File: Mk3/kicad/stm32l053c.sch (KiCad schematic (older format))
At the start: 44 parts, among them J1 GND, J10 3V3, J2 GND, J3 TX, J4 GND, J5 TEST_1P, J6 TEST_1P, J7 TEST_1P, J8 RX, J9 3V3, P1 SWD, U1 AP2112, U2 STM32L053C8_LQFP48, U3 ADS1015, U4 UFL_SMA, U5 RFM92/95

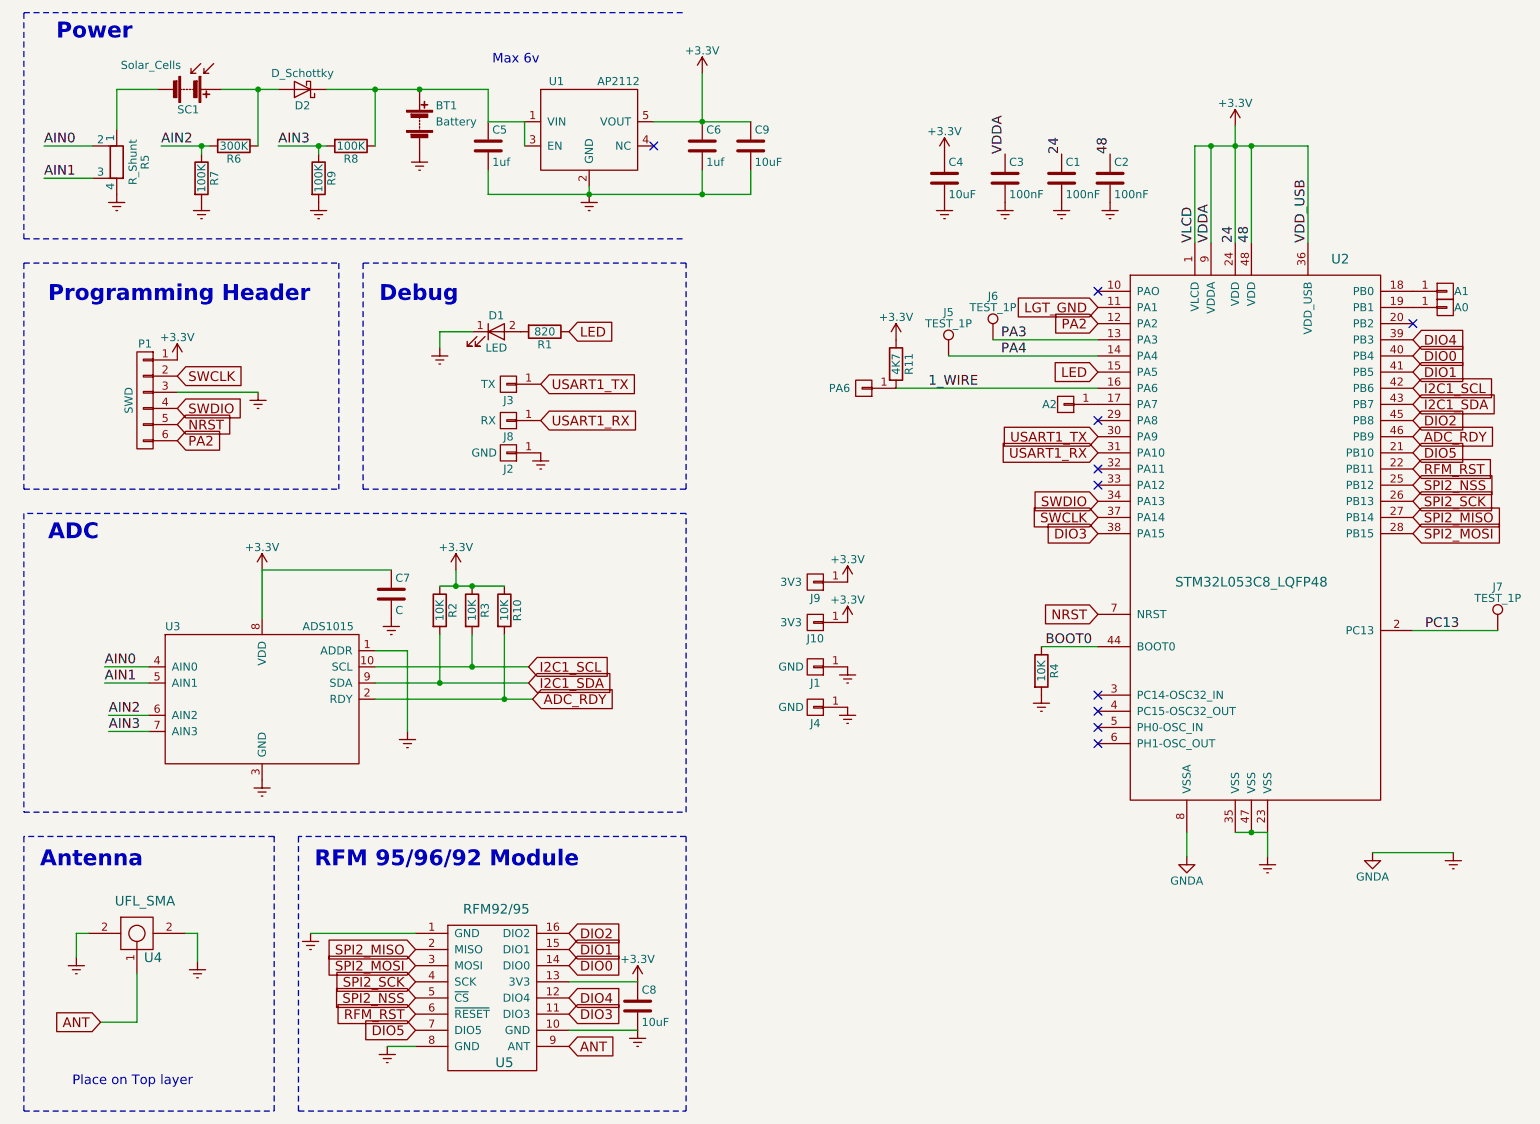
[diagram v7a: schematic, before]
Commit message: I2C header
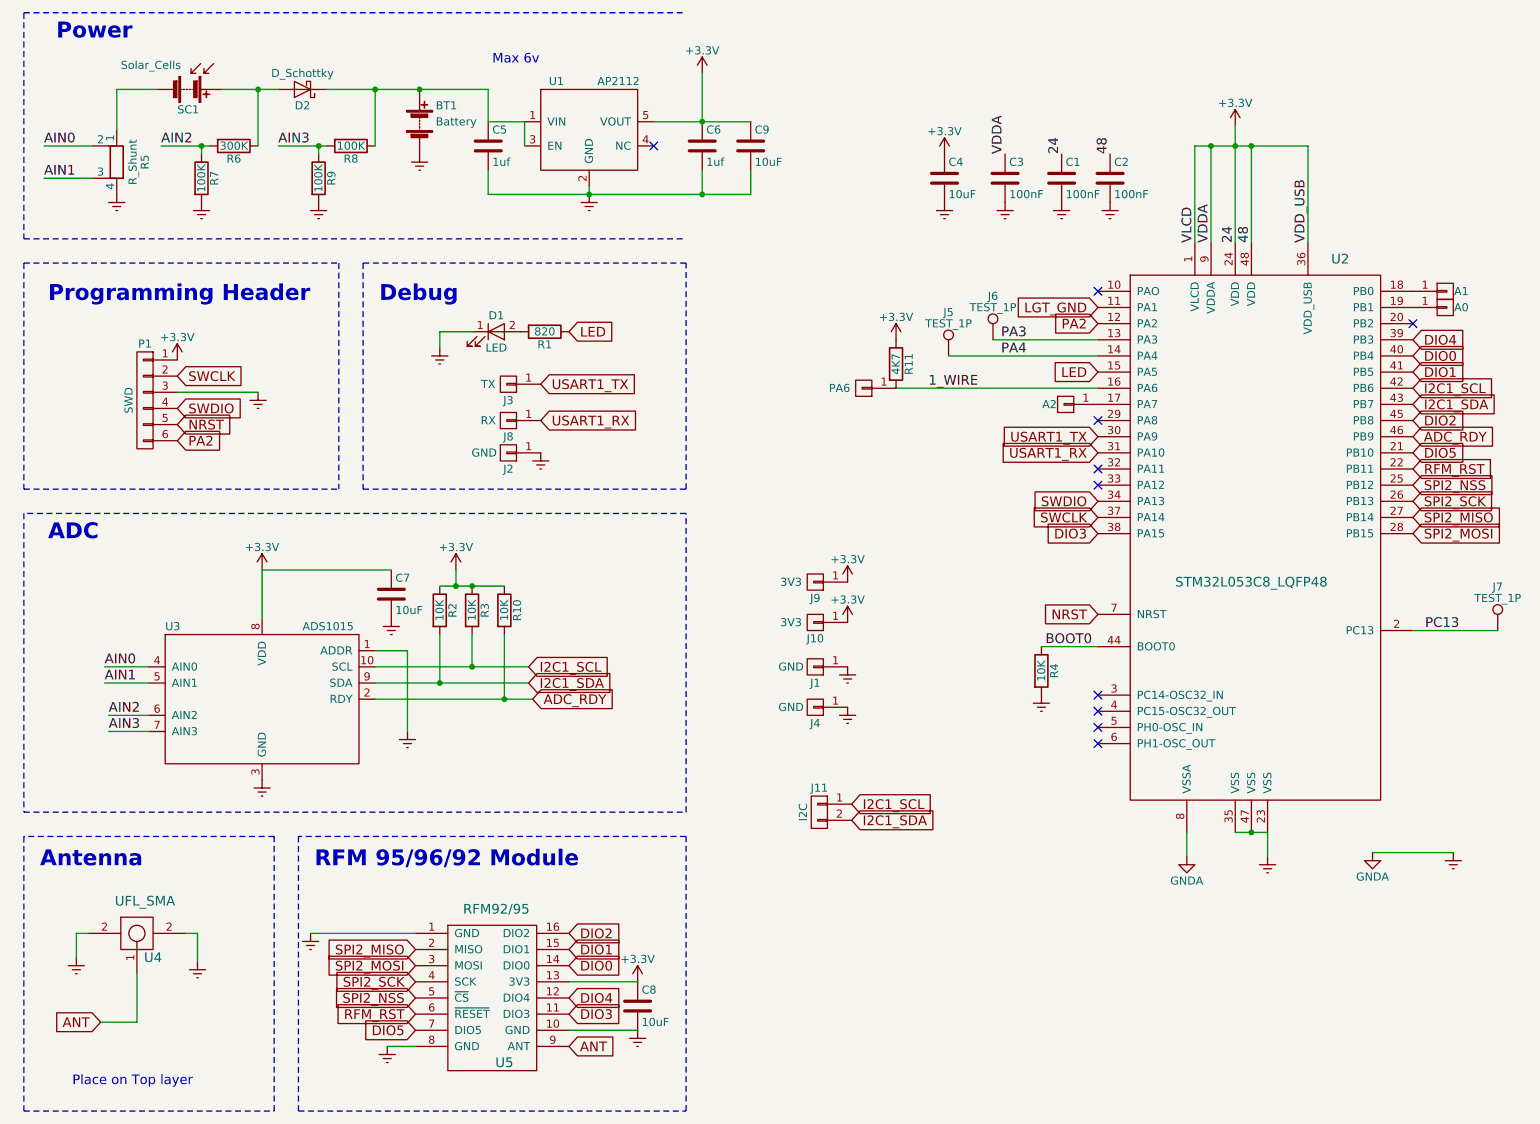
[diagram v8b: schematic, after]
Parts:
- added J11: I2C, Pin_Headers:Pin_Header_Straight_1x02_Pitch2.54mm, symbol CONN_01X02
- C7: value C -> 10uF
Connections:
- net I2C1_SCL: now also J11.1 (P1)
- net I2C1_SDA: now also J11.2 (P2)
